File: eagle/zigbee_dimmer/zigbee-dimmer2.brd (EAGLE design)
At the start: 100 x 80 mm, 4 parts, among them U2 CREE_ZIGBEE

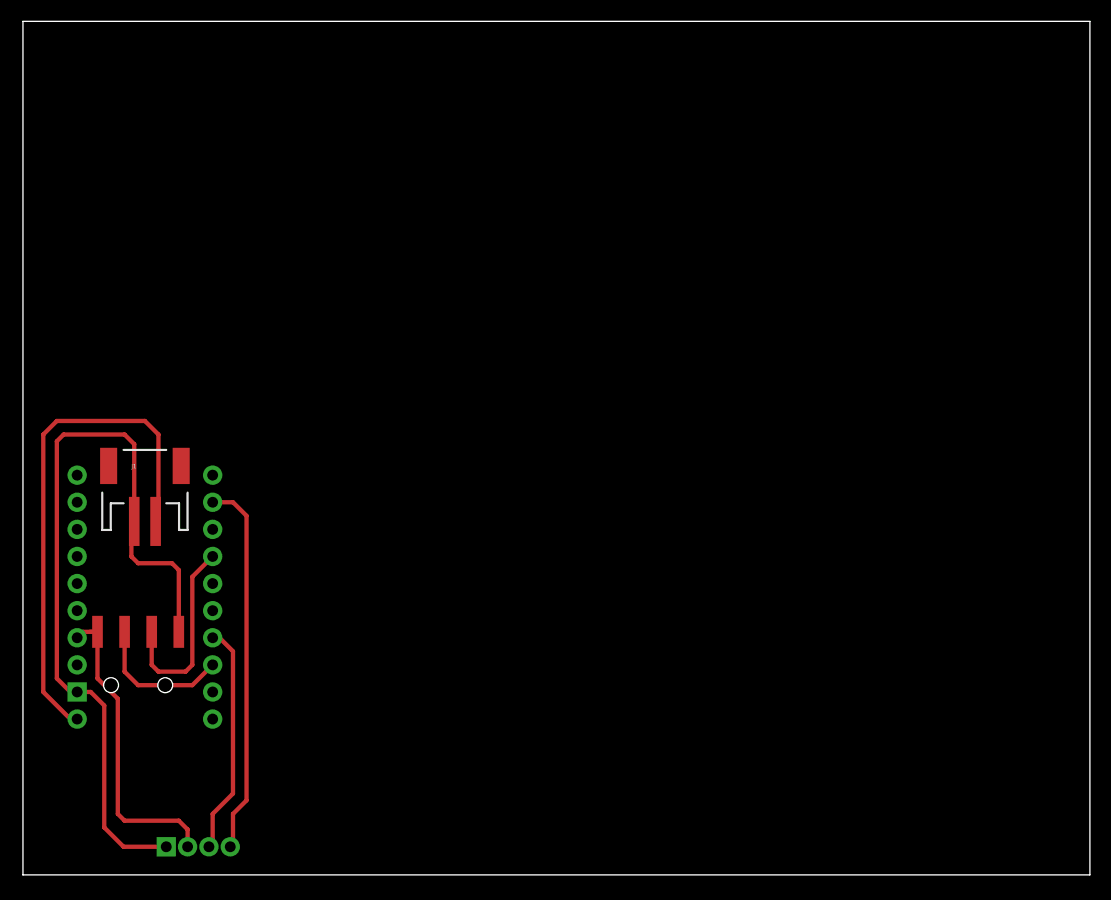
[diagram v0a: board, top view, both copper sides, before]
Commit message: changes for board milling
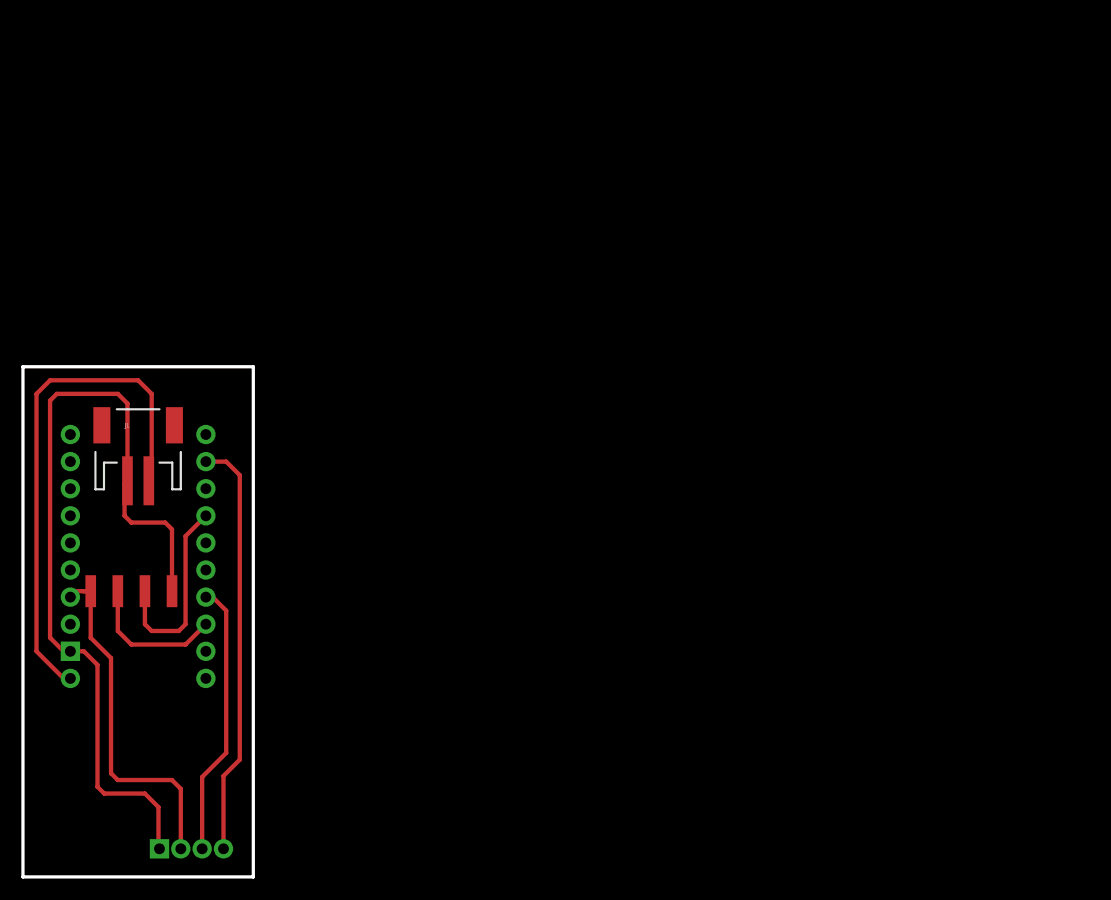
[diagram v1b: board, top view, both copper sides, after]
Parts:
- moved J1 3.86 mm to (10.8, 40.6)
- moved JP1 3.86 mm to (10.2, 21.6)
- moved U$1 3.86 mm to (10.8, 29.8)
- moved U2 0.66 mm to (10.8, 0.45)
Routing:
- net PWM: track 21.7 -> 25.7 mm
- net 3V3: track 29.5 -> 33.5 mm
- net ONOFF: track 35.4 -> 39.4 mm
- net GND: track 75.0 -> 78.9 mm
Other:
- board size 100 x 80 mm -> 21.6 x 47.8 mm
